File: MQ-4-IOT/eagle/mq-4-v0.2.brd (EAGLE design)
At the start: 22.5 x 30.5 mm, 3 parts

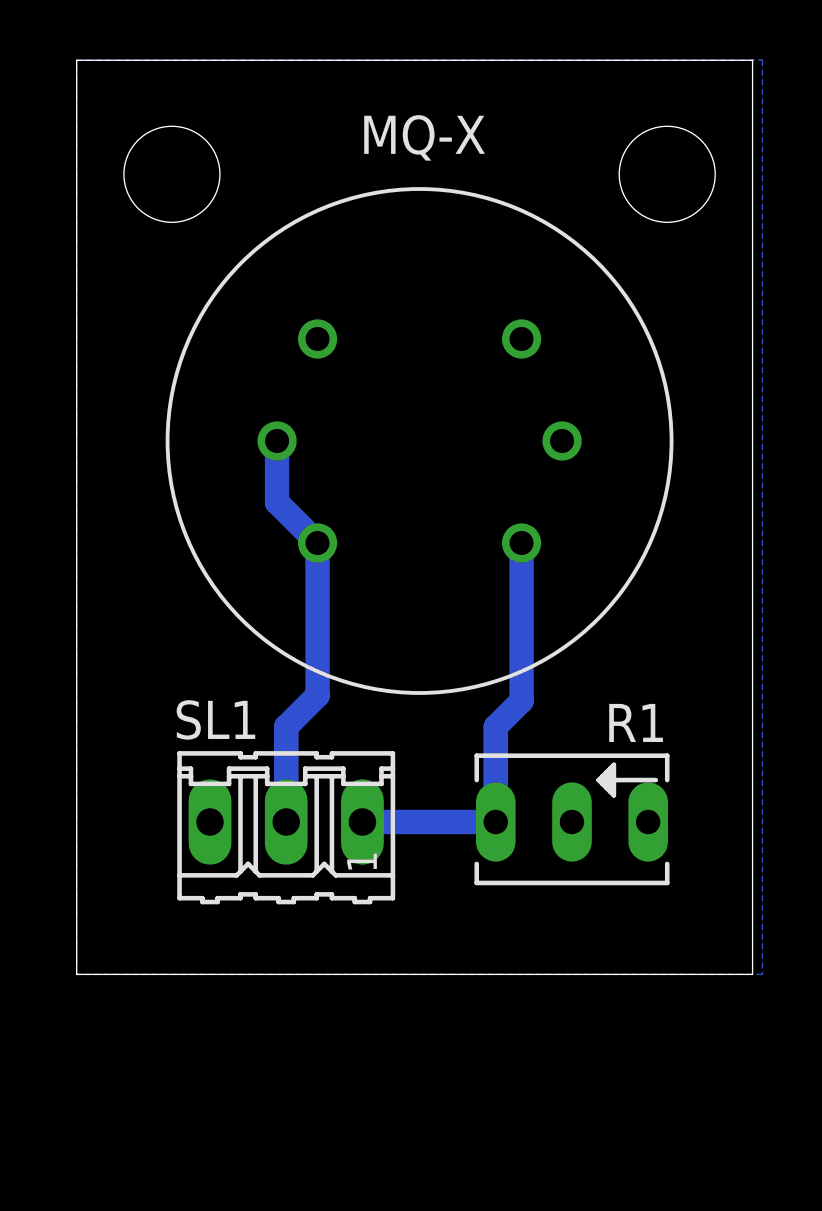
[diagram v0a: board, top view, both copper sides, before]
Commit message: Added enclosure top half.
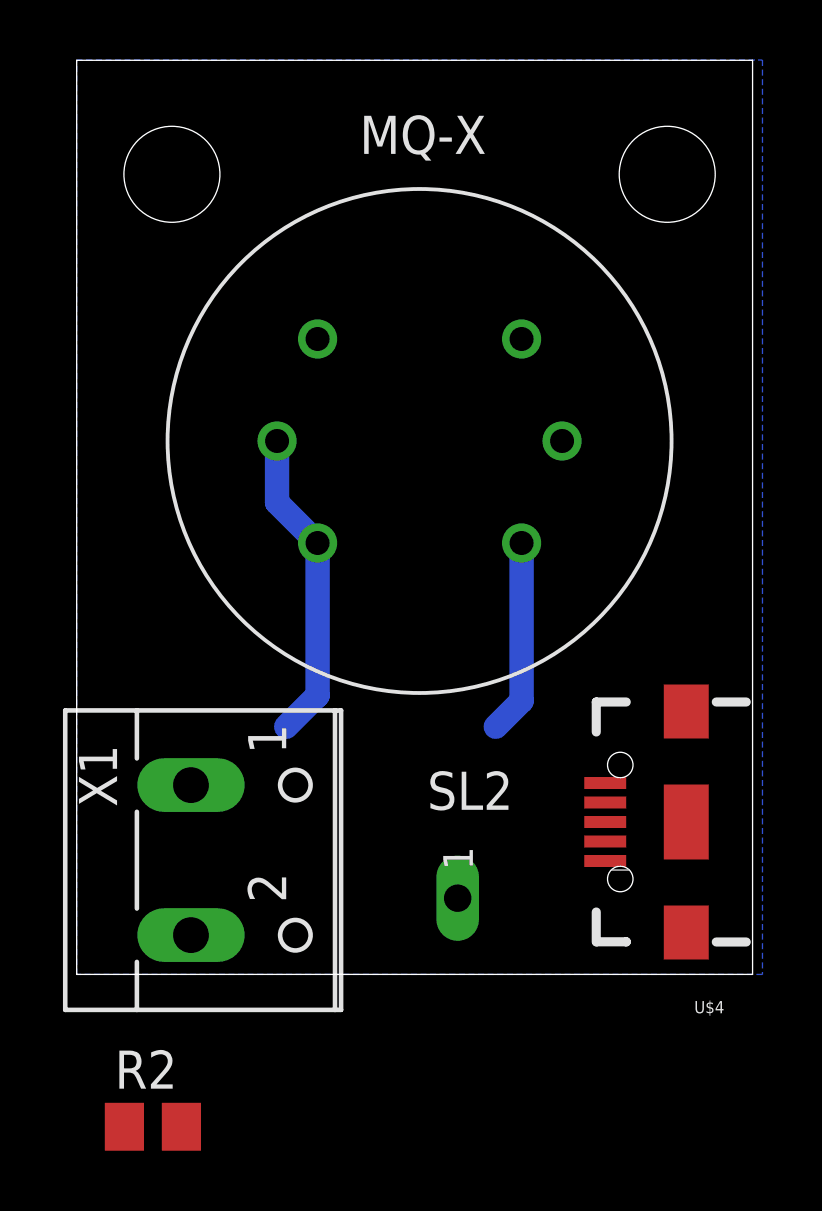
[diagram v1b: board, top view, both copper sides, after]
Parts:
- removed R1: 50k, pot:B64Y
- removed SL1: (no value), con-amp-quick:03P
- added R2: 10k, rcl:M0805
- added SL2: (no value), pads:02P
- added U$4: (no value), Testing:USB-AB-MICRO-SMD_V02_BOSS
- added X1: (no value), con-wago-500:W237-102
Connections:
- net GND: now also R2.2, U$4.GND1, X1.1; no longer R1.E, R1.S, SL1.3
- net VCC: now also U$4.VBUS1, X1.2; no longer SL1.2
- net VOUT: now also R2.1, SL2.1; no longer R1.A, SL1.1
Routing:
- net VOUT: track 14.1 -> 6.48 mm
- net VCC: track 13.7 -> 10.5 mm

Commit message: Added CAM files.
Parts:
- removed R2: 10k, rcl:M0805
- removed U$4: (no value), Testing:USB-AB-MICRO-SMD_V02_BOSS
- added R4: 10k, rcl:0207/10
- moved SL2 6.35 mm to (17.8, 7.62)
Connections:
- net GND: now also R4.1, X1.2; no longer R2.2, U$4.GND1, X1.1
- net VCC: now also X1.1; no longer U$4.VBUS1, X1.2
- net VOUT: now also R4.2; no longer R2.1
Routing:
- net VCC: track 10.5 -> 0.00 mm
- net VOUT: track 6.48 -> 0.00 mm
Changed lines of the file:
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@@
 <setting verticaltext="up"/>
 </settings>
-<grid distance="0.05" unitdist="inch" unit="mm" style="lines" multiple="1" display="yes" altdistance="0.025" altunitdist="inch" altunit="inch"/>
+<grid distance="0.635" unitdist="mm" unit="mm" style="lines" multiple="1" display="yes" altdistance="0.025" altunitdist="inch" altunit="mm"/>
 <layers>
 <layer number="1" name="Top" color="4" fill="1" visible="yes" active="yes"/>
@@
 </variantdefs>
 <classes>
-<class number="0" name="default" width="0.1524" drill="0">
-<clearance class="0" value="0.1524"/>
+<class number="0" name="default" width="0.9144" drill="0.254">
+<clearance class="0" value="0.508"/>
 </class>
-<class number="1" name="Power" width="0.4064" drill="0.6096">
-<clearance class="1" value="0.1524"/>
+<class number="1" name="GND" width="0.9144" drill="0.254">
+<clearance class="1" value="0.508"/>
 </class>
 </classes>
@@
 <autorouter>
 <pass name="Default">
-<param name="RoutingGrid" value="6.25mil"/>
+<param name="RoutingGrid" value="0.125mm"/>
 <param name="AutoGrid" value="1"/>
-<param name="Efforts" value="0"/>
+<param name="Efforts" value="2"/>
 <param name="TopRouterVariant" value="1"/>
 <param name="tpViaShape" value="round"/>
@@
 <elements>
 <element name="U$1" library="mq-x" package="MQ-4" value="MQ-4" x="11.43" y="17.78" smashed="yes"/>
-<element name="U$4" library="Testing" package="USB-AB-MICRO-SMD_V02_BOSS" value="" x="20.32" y="5.08" rot="R180"/>
 <element name="X1" library="con-wago-500" package="W237-102" value="" x="5.08" y="3.81" rot="R270">
 <attribute name="MF" value="" x="17.78" y="15.24" size="1.778" layer="27" rot="R270" display="off"/>
@@
 <attribute name="OC_NEWARK" value="70K9898" x="17.78" y="15.24" size="1.778" layer="27" rot="R270" display="off"/>
 </element>
-<element name="SL2" library="pads" package="02P" value="" x="13.97" y="2.54"/>
-<element name="R2" library="rcl" package="M0805" value="10k" x="2.54" y="-5.08"/>
+<element name="SL2" library="pads" package="02P" value="" x="17.78" y="7.62"/>
+<element name="R4" library="rcl" package="0207/10" value="10k" x="15.24" y="3.81" rot="R180"/>
 </elements>
 <signals>
@@
 <contactref element="U$1" pad="H"/>
 <contactref element="U$1" pad="A1"/>
-<wire x1="6.68" y1="17.78" x2="6.68" y2="15.73" width="0.8128" layer="16"/>
-<wire x1="6.68" y1="15.73" x2="8.03" y2="14.38" width="0.8128" layer="16"/>
-<wire x1="8.03" y1="14.38" x2="8.03" y2="9.3" width="0.8128" layer="16"/>
-<wire x1="8.03" y1="9.3" x2="6.985" y2="8.255" width="0.8128" layer="16"/>
-<contactref element="X1" pad="2"/>
-<contactref element="U$4" pad="VBUS1"/>
-<wire x1="8.03" y1="9.3" x2="17.62" y2="3.78" width="0" layer="19" extent="1-16"/>
-<wire x1="3.81" y1="1.31" x2="6.985" y2="8.255" width="0" layer="19" extent="16-16"/>
+<contactref element="X1" pad="1"/>
+<wire x1="8.03" y1="14.38" x2="6.68" y2="17.78" width="0" layer="19" extent="1-1"/>
+<wire x1="3.81" y1="6.31" x2="8.03" y2="14.38" width="0" layer="19" extent="1-1"/>
 </signal>
 <signal name="GND" class="1">
 <contactref element="U$1" pad="H1"/>
 <polygon width="0.4064" layer="16">
-<vertex x="0" y="0"/>
+<vertex x="0" y="-1.27"/>
 <vertex x="0" y="30.48"/>
 <vertex x="22.86" y="30.48"/>
-<vertex x="22.86" y="0"/>
+<vertex x="22.86" y="-1.27"/>
 </polygon>
-<contactref element="U$4" pad="GND1"/>
-<contactref element="X1" pad="1"/>
-<contactref element="R2" pad="2"/>
-<wire x1="17.62" y1="6.38" x2="16.18" y2="17.78" width="0" layer="19" extent="1-1"/>
-<wire x1="3.81" y1="6.31" x2="17.62" y2="6.38" width="0" layer="19" extent="1-1"/>
-<wire x1="3.49" y1="-5.08" x2="3.81" y2="6.31" width="0" layer="19" extent="1-1"/>
+<contactref element="R4" pad="1"/>
+<contactref element="X1" pad="2"/>
 </signal>
 <signal name="VOUT">
 <contactref element="U$1" pad="B1"/>
-<wire x1="14.83" y1="14.38" x2="14.83" y2="9.115" width="0.8128" layer="16"/>
-<wire x1="14.83" y1="9.115" x2="13.97" y2="8.255" width="0.8128" layer="16"/>
 <contactref element="SL2" pad="1"/>
-<contactref element="R2" pad="1"/>
-<wire x1="12.7" y1="2.54" x2="13.97" y2="8.255" width="0" layer="19" extent="16-16"/>
-<wire x1="1.59" y1="-5.08" x2="12.7" y2="2.54" width="0" layer="19" extent="1-1"/>
+<contactref element="R4" pad="2"/>
+<wire x1="16.51" y1="7.62" x2="14.83" y2="14.38" width="0" layer="19" extent="1-1"/>
+<wire x1="10.16" y1="3.81" x2="16.51" y2="7.62" width="0" layer="19" extent="1-1"/>
 </signal>
 </signals>

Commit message: Board update.
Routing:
- net VOUT: track 0.00 -> 15.4 mm
- net VCC: track 0.00 -> 13.8 mm
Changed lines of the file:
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@@
 <setting verticaltext="up"/>
 </settings>
-<grid distance="0.635" unitdist="mm" unit="mm" style="lines" multiple="1" display="yes" altdistance="0.025" altunitdist="inch" altunit="mm"/>
+<grid distance="0.3175" unitdist="mm" unit="mm" style="lines" multiple="1" display="yes" altdistance="0.3175" altunitdist="mm" altunit="mm"/>
 <layers>
 <layer number="1" name="Top" color="4" fill="1" visible="yes" active="yes"/>
@@
 <contactref element="U$1" pad="A1"/>
 <contactref element="X1" pad="1"/>
-<wire x1="8.03" y1="14.38" x2="6.68" y2="17.78" width="0" layer="19" extent="1-1"/>
-<wire x1="3.81" y1="6.31" x2="8.03" y2="14.38" width="0" layer="19" extent="1-1"/>
+<wire x1="6.68" y1="17.78" x2="6.68" y2="15.73" width="1.27" layer="16"/>
+<wire x1="6.68" y1="15.73" x2="8.03" y2="14.38" width="1.27" layer="16"/>
+<wire x1="8.03" y1="14.38" x2="8.03" y2="10.53" width="1.27" layer="16"/>
+<wire x1="8.03" y1="10.53" x2="3.81" y2="6.31" width="1.27" layer="16"/>
 </signal>
 <signal name="GND" class="1">
@@
 <contactref element="SL2" pad="1"/>
 <contactref element="R4" pad="2"/>
-<wire x1="16.51" y1="7.62" x2="14.83" y2="14.38" width="0" layer="19" extent="1-1"/>
-<wire x1="10.16" y1="3.81" x2="16.51" y2="7.62" width="0" layer="19" extent="1-1"/>
+<wire x1="14.83" y1="14.38" x2="14.83" y2="9.3" width="1.27" layer="16"/>
+<wire x1="14.83" y1="9.3" x2="16.51" y2="7.62" width="1.27" layer="16"/>
+<wire x1="10.16" y1="3.81" x2="12.7" y2="3.81" width="1.27" layer="16"/>
+<wire x1="12.7" y1="3.81" x2="16.51" y2="7.62" width="1.27" layer="16"/>
 </signal>
 </signals>
